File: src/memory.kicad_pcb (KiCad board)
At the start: 2 copper layers, 35 x 45 mm, 8 parts, among them Q1 NPN, Q2 NPN, SW1 SW_Push, SW2 SW_Push

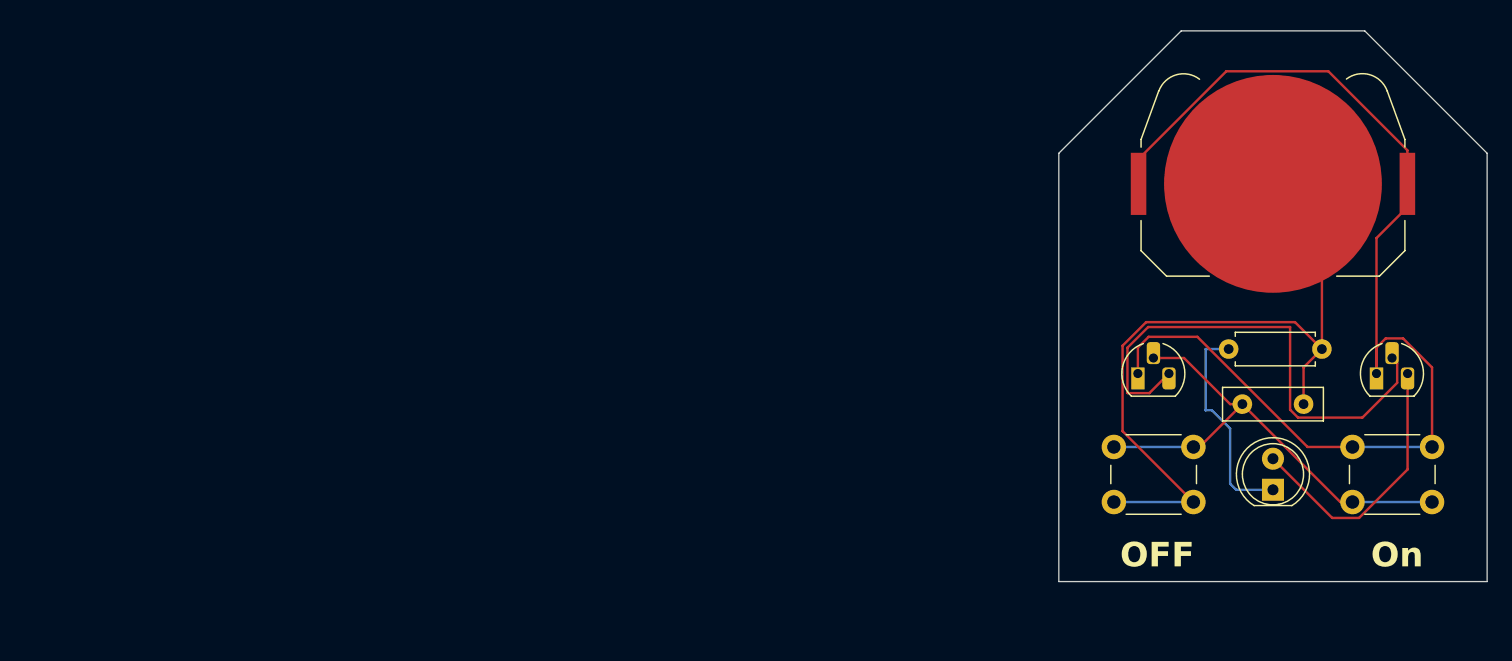
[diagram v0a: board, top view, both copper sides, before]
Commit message: Update entire PCB
README not updated
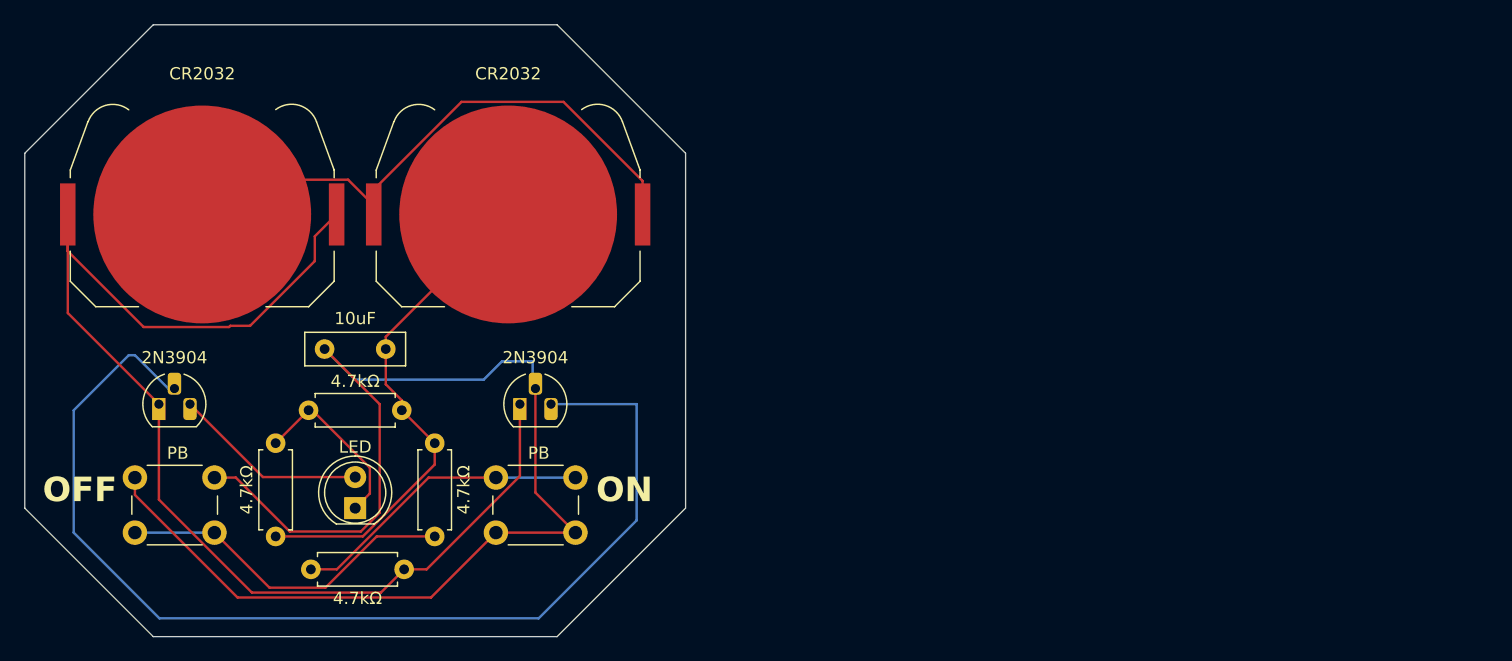
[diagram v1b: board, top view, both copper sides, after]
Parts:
- removed C1: C, Capacitor_THT:C_Disc_D8.0mm_W2.5mm_P5.00mm
- removed D1: LED, LED_THT:LED_D5.0mm
- removed Q1, Q2: NPN, Package_TO_SOT_THT:TO-92L_HandSolder
- removed R1: R, Resistor_THT:R_Axial_DIN0207_L6.3mm_D2.5mm_P7.62mm_Horizontal
- removed SW1, SW2: SW_Push, Button_Switch_THT:SW_PUSH_6mm
- added 10uF: C, Capacitor_THT:C_Disc_D8.0mm_W2.5mm_P5.00mm, F.Cu at (110.0, 111.0)
- added 2N3904: NPN, Package_TO_SOT_THT:TO-92L_HandSolder, F.Cu at (126.0, 115.5)
- added 2N3904: NPN, Package_TO_SOT_THT:TO-92L_HandSolder, F.Cu at (96.5, 115.5)
- added 4.7kΩ: R, Resistor_THT:R_Axial_DIN0207_L6.3mm_D2.5mm_P7.62mm_Horizontal, F.Cu at (108.7, 116.0)
- added CR2032: Battery_Cell, Battery:BatteryHolder_Keystone_3034_1x20mm, F.Cu at (125.0, 100.0)
- added LED: LED, LED_THT:LED_D5.0mm, F.Cu at (112.5, 124.0)
- added OFF: SW_Push, Button_Switch_THT:SW_PUSH_6mm, F.Cu at (94.5, 121.5)
- added ON: SW_Push, Button_Switch_THT:SW_PUSH_6mm, F.Cu at (124.0, 121.5)
- added R: 4.7kΩ, Resistor_THT:R_Axial_DIN0207_L6.3mm_D2.5mm_P7.62mm_Horizontal, F.Cu at (119.0, 126.3)
- added R: 4.7kΩ, Resistor_THT:R_Axial_DIN0207_L6.3mm_D2.5mm_P7.62mm_Horizontal, F.Cu at (106.0, 118.7)
- added R\: 4.7kΩ, Resistor_THT:R_Axial_DIN0207_L6.3mm_D2.5mm_P7.62mm_Horizontal, F.Cu at (108.9, 129.0)
- moved BT1 87.5 mm to (100.0, 100.0)
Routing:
- net Net-(Q1-B): track 39.6 -> 108.4 mm
- net Net-(Q1-E): track 40.9 -> 89.9 mm
- net Net-(BT2--): track 0.00 -> 41.7 mm
- net Net-(R4-Pad1): track 0.00 -> 28.1 mm
- net Net-(R3-Pad1): track 0.00 -> 24.7 mm
- net Net-(BT1--): track 60.0 -> 49.2 mm
- net Net-(BT1-+): track 93.6 -> 101.4 mm
- net Net-(D1-A): track 22.5 -> 16.0 mm
- net Net-(D1-K): track 17.7 -> 14.6 mm
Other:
- board size 35 x 45 mm -> 54 x 50 mm
- board text added: "CR2032"
- board text added: "PB"
- board text removed: "OFF"
- board text removed: "On"

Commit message: Update back of PCB
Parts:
- added G***: LOGO, LOGO, B.Cu at (125.0, 100.0)
- added G***: LOGO, LOGO, B.Cu at (100.0, 100.0)
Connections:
- BT1 pad 1: Net-(BT1-+) -> (no net)
- BT1 pad 2: Net-(BT1--) -> (no net)
